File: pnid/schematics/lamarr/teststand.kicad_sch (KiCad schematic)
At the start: 72 parts

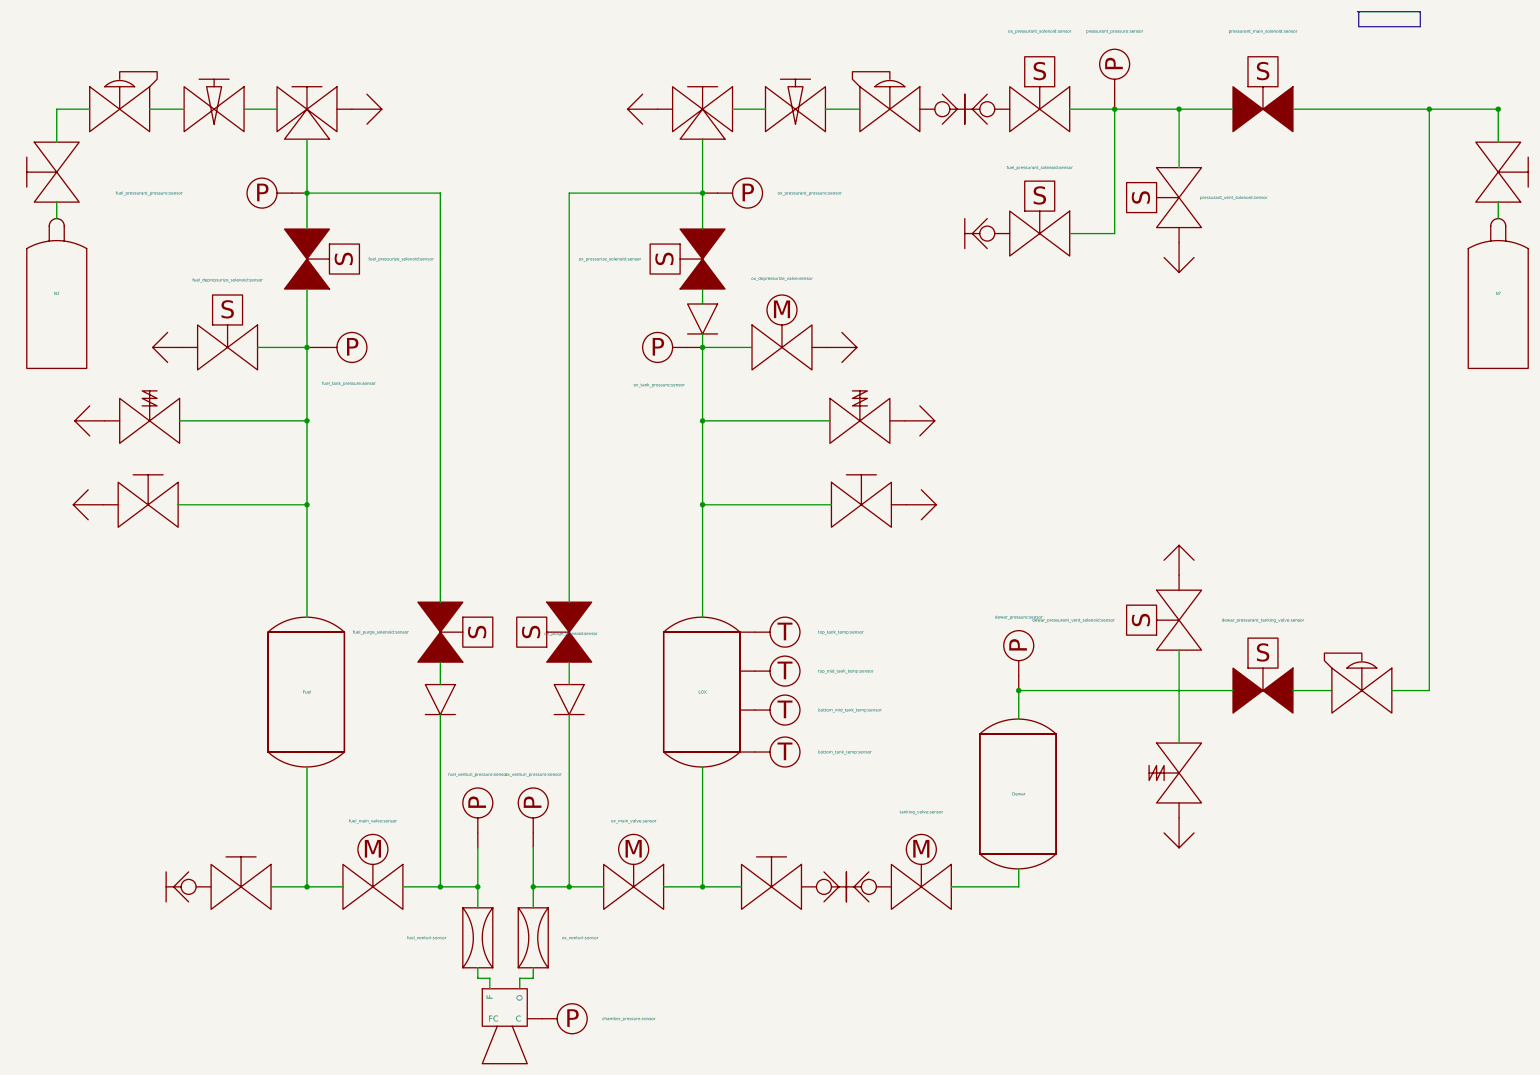
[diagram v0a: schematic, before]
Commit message: update schematics to kicad 8
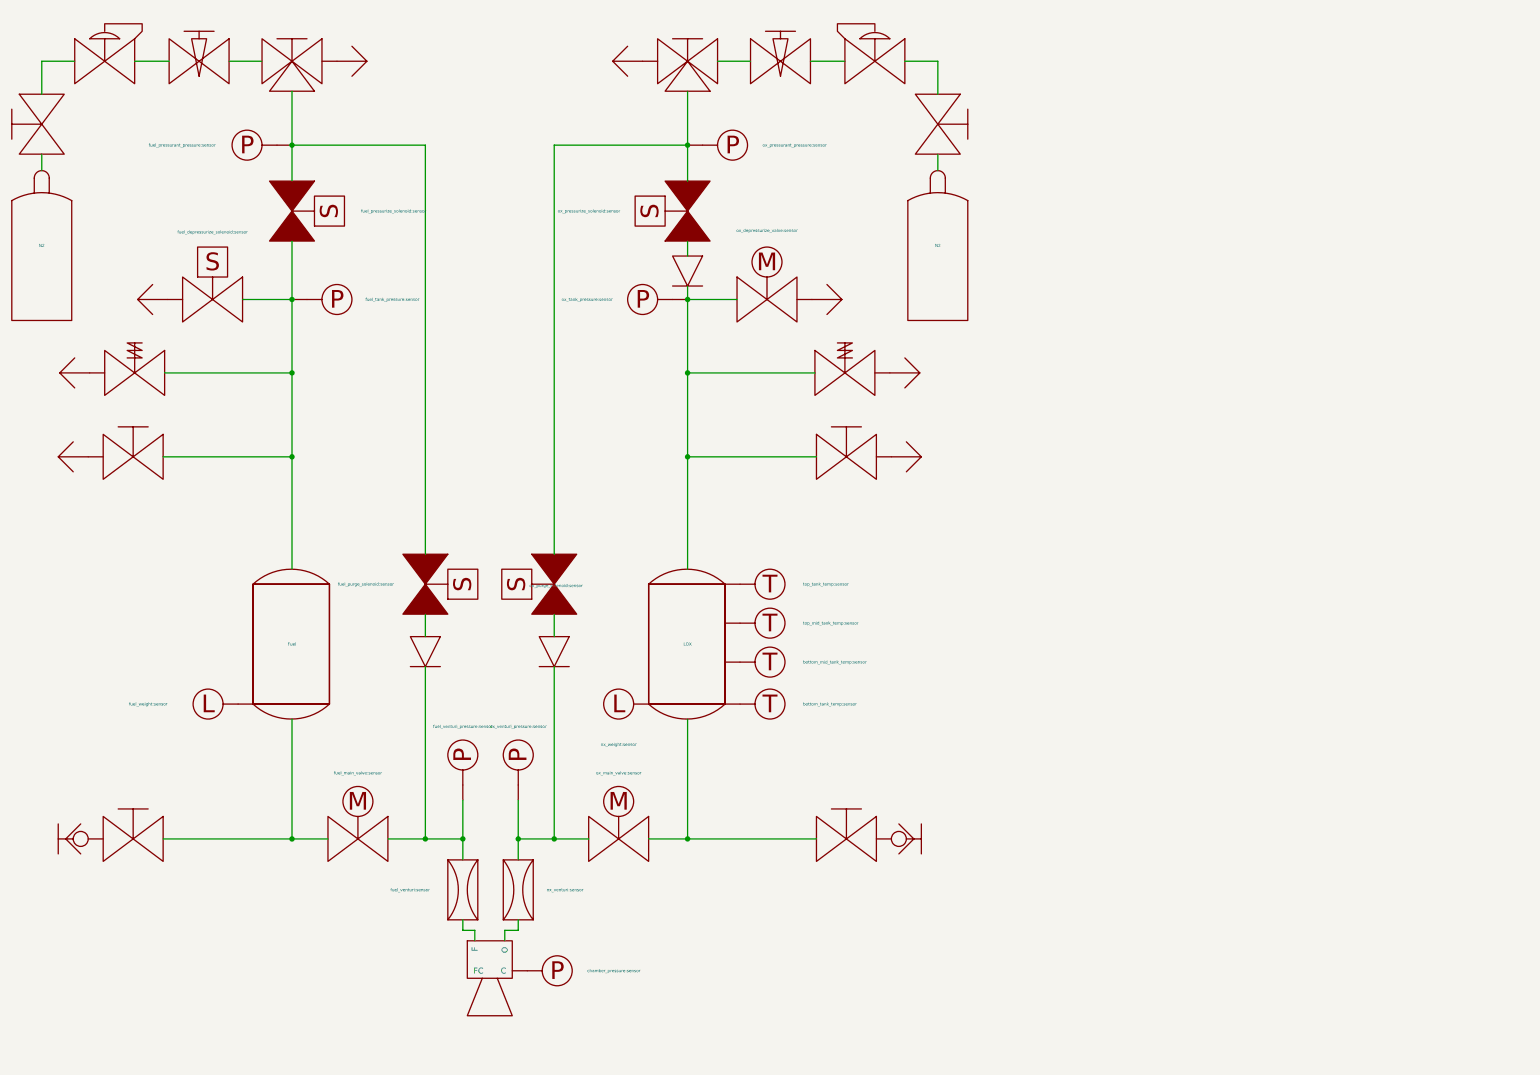
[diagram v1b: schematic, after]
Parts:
- removed Dewar: dewar_fill_level:sensor, symbol PnID-Lib:Tank_Slim
- removed DewarOverPressureValve?: DewarOverPressureValve, symbol PnID-Lib:Valve_OverPressure
- removed DewarPressureRegulator?: DewarPressureRegulator, symbol PnID-Lib:PressureRegulator
- removed DewarQuickConnect?: DewarQuickConnect, symbol PnID-Lib:QuickConnect_Half
- removed N?: N2, symbol PnID-Lib:GasBottle
- removed QuickConnect?: QuickConnect_Half, symbol PnID-Lib:QuickConnect_Half
- removed Vent? (x4): Vent, symbol PnID-Lib:Vent
- removed dewar_pressurant_tanking_valve?: dewar_pressurant_tanking_valve:sensor, symbol PnID-Lib:Valve_Solenoid_NC
- removed dewar_pressurant_vent_solenoid?: dewar_pressurant_vent_solenoid:sensor, symbol PnID-Lib:Valve_Solenoid_NO
- removed dewar_pressure?: dewar_pressure:sensor, symbol PnID-Lib:Sensor_Pressure
- removed fuel_pressurant_solenoid?: fuel_pressurant_solenoid:sensor, symbol PnID-Lib:Valve_Solenoid_NO
- removed fuel_quick_connect?: fuel_quick_connect, symbol PnID-Lib:QuickConnect_Half
- removed ox_pressurant_solenoid?: ox_pressurant_solenoid:sensor, symbol PnID-Lib:Valve_Solenoid_NO
- removed ox_quick_connect?: ox_quick_connect, symbol PnID-Lib:QuickConnect_Half
- removed pressurant_main_solenoid?: pressurant_main_solenoid:sensor, symbol PnID-Lib:Valve_Solenoid_NC
- removed pressurant_pressure?: pressurant_pressure:sensor, symbol PnID-Lib:Sensor_Pressure
- removed pressurant_vent_solenoid?: pressurant_vent_solenoid:sensor, symbol PnID-Lib:Valve_Solenoid_NO
- removed tanking_valve?: tanking_valve:sensor, symbol PnID-Lib:Valve_Servo
- added N2: N2, symbol PnID-Lib:GasBottle
- added Vent?: Vent, symbol PnID-Lib:Vent
- added fuel_weight: fuel_weight:sensor, symbol PnID-Lib:Sensor_Load
- added ox_weight: ox_weight:sensor, symbol PnID-Lib:Sensor_Load_Short
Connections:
- net at engine.~ (O): now also fuel_venturi.~
- net at ox_venturi.~: now also CheckValve?.~, ox_main_valve.~, ox_venturi_pressure.~; no longer engine.~ (O)
- net at fuel_venturi.~: now also CheckValve?.~, fuel_main_valve.~, fuel_venturi_pressure.~; no longer engine.~ (O)
- net at ox_manual_valve.~: now also N2.~
- net at ox_pressure_regulator.~: now also ox_manual_valve.~
- net at ox_manual_vent_valve.~: now also Vent?.~
- net at ox_needle_valve.~: now also fuel_manual_3way?.~; no longer ox_pressure_regulator.~
- new net: fuel_manual_3way?.~, ox_pressurant_pressure:sensor.~, ox_pressurize_solenoid.~, ox_purge_solenoid.~
- new net: fuel_manual_3way.~, fuel_pressurant_pressure.~, fuel_pressurize_solenoid.~, fuel_purge_solenoid.~
- new net: Fuel.~, fuel_depressurize_solenoid.~, fuel_manual_vent_valve.~, fuel_pressurize_solenoid.~, fuel_safety_valve.~, fuel_tank_pressure.~
- new net: CheckValve?.~, LOX.~, ox_depressurize_valve.~, ox_manual_vent_valve.~, ox_safety_valve.~, ox_tank_pressure.~
- new net: LOX.~, ox_main_valve.~, ox_manual_tanking_valve.~
- new net: Fuel.~, fuel_main_valve.~, fuel_manual_tanking_valve.~
- new net: engine.~ (O), ox_venturi.~
- new net: ox_needle_valve.~, ox_pressure_regulator.~
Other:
- moved on the sheet: Fuel, LOX, N2
